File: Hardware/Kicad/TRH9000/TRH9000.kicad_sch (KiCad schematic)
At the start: 10 parts, among them U4 74VHC138, U5 T.I_SN74AHCT32D

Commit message: Started routing the PCB, adding cut-outs to separate the analog from digital signal-domains.
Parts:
- removed C11, C12: C_CC0805JPX7R9BB104, Capacitor_SMD:C_0805_2012Metric, symbol LRJ-parts:C_CC0805JPX7R9BB104
- removed C25, C26, C27: C_CL21B105KBFNNNF, Capacitor_SMD:C_0805_2012Metric_Pad1.18x1.45mm_HandSolder, symbol LRJ-parts:C_CL21B105KBFNNNF
- added C23: C_CL21B106KOQNNNE, Capacitor_SMD:C_0805_2012Metric, symbol LRJ-parts:C_CL21B106KOQNNNE
- added LOGO1: Logo_Open_Hardware_Small, Symbol:OSHW-Logo2_14.6x12mm_SilkScreen, symbol Graphic:Logo_Open_Hardware_Small
- BUS1: value MSX_SLOT_EDGE-CON -> MSX-CONN_L-P; footprint trh9000:msx_cartridge -> trh9000:msx_edge-conn-LP; symbol TRH9000:MSX_SLOT_EDGE-CON -> TRH9000:MSX-CONN_L-P
- Cart1: footprint trh9000:MSX-cart-dummy -> trh9000:MSX-cart-dummy_RA
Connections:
- net +5V: now also C23.1
- net GND: now also C23.2
- net ~{Y6}: now reaches U4.9 (~{Y6}), U5.2 (1B), U5.5 (2B)
- removed net +12V: BUS1.48 (+12V)
- removed net -12V: BUS1.50 (-12V)
- removed net ~{RFSH}: BUS1.6 (~{RFSH})
- no-connect marks 11 -> 12

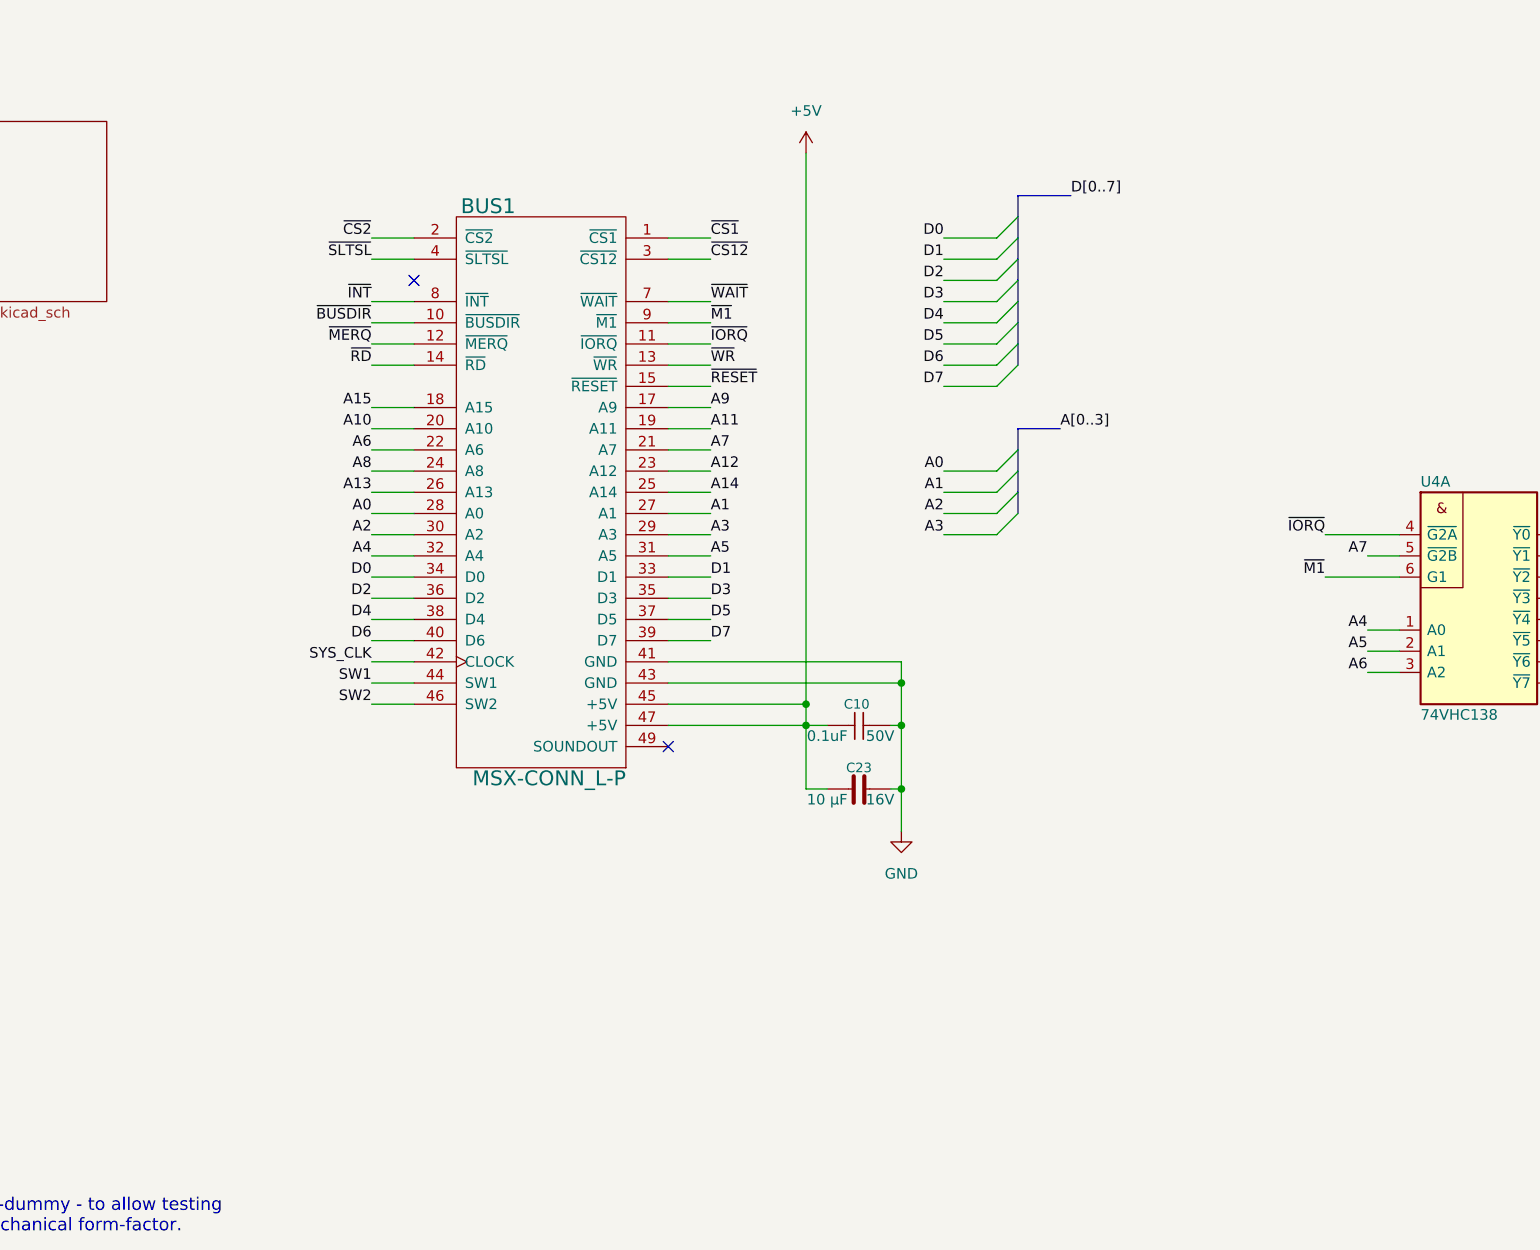
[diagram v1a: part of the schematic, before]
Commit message: More routing of the analog portion. Added 3D-models for the VGA and Scart connectors.
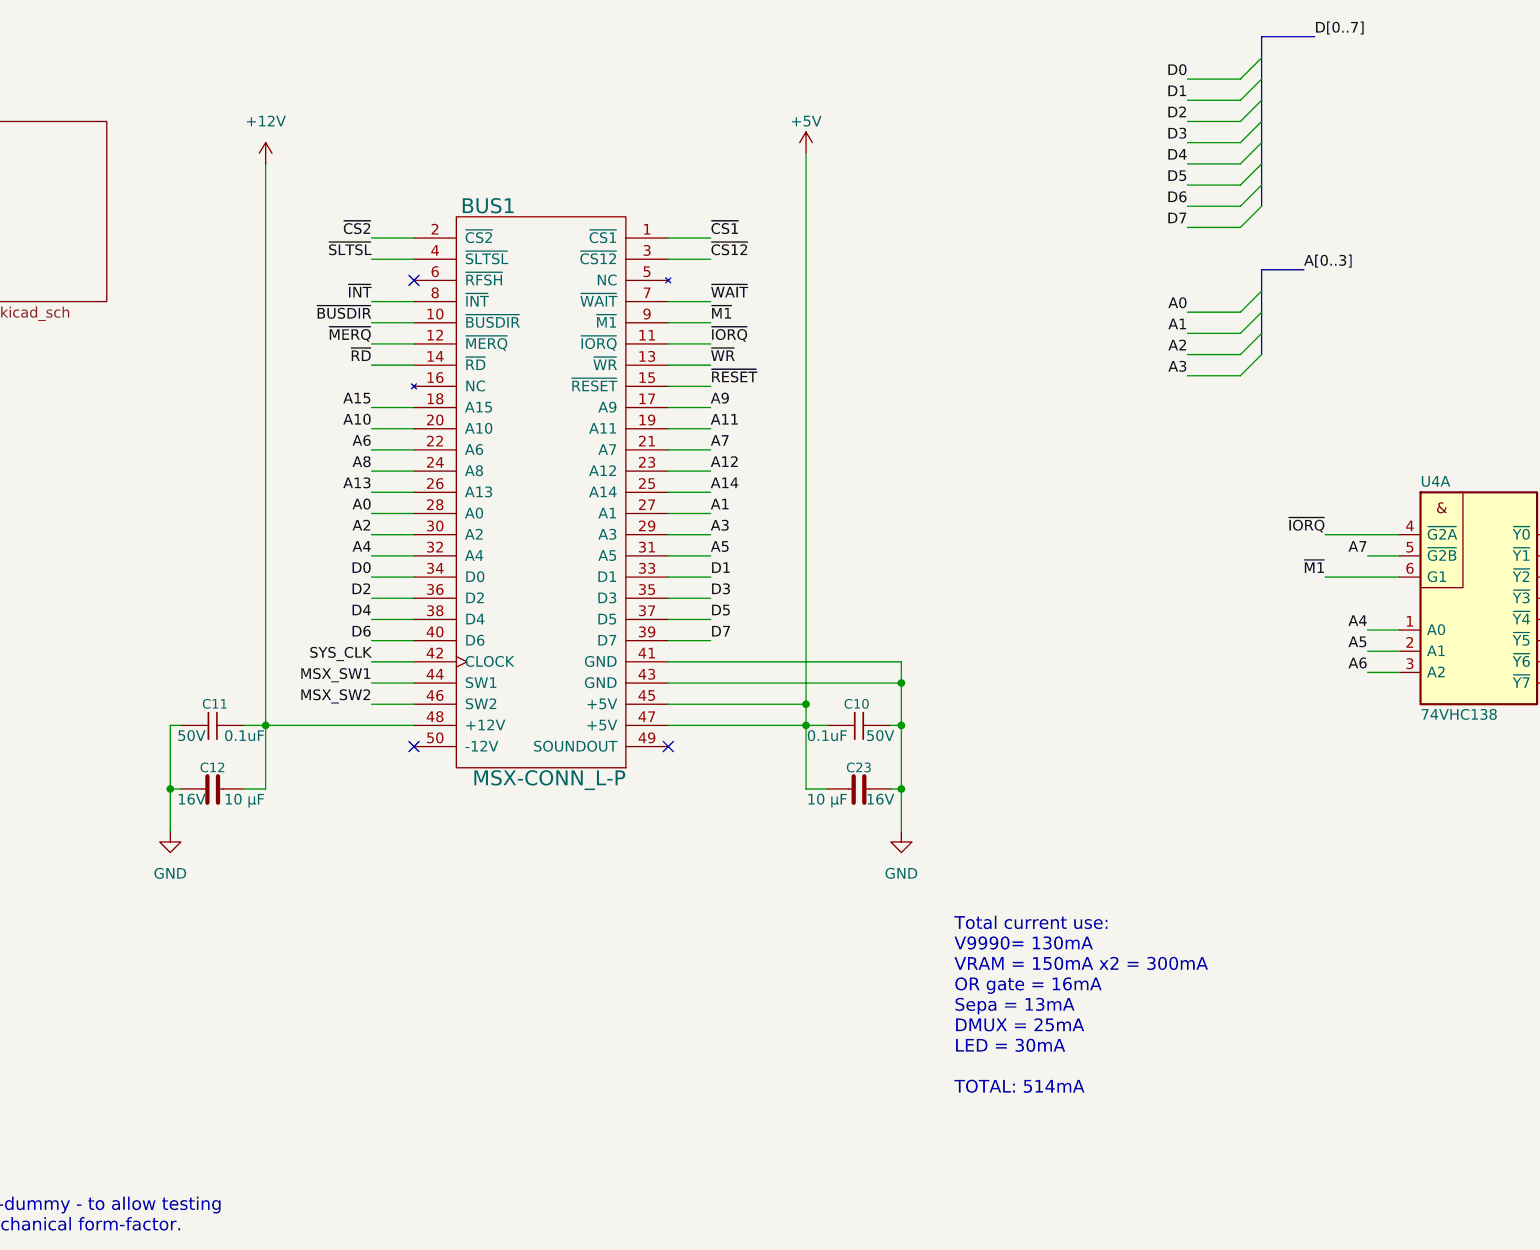
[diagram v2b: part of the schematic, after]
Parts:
- added C11: C_CC0805JPX7R9BB104, Capacitor_SMD:C_0805_2012Metric, symbol LRJ-parts:C_CC0805JPX7R9BB104
- added C12: C_CL21B106KOQNNNE, Capacitor_SMD:C_0805_2012Metric, symbol LRJ-parts:C_CL21B106KOQNNNE
- BUS1: footprint trh9000:msx_edge-conn-LP -> trh9000:msx_cart_edge-conn; symbol TRH9000:MSX-CONN_L-P -> TRH9000:MSX_SLOT_EDGE-CON
- C10: Price €0,14 -> (none)
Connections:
- net GND: now also C11.2, C12.2
- net SW1 renamed MSX_SW1
- net SW2 renamed MSX_SW2
- new net +12V: BUS1.48 (+12V), C11.1, C12.1
- no-connect marks 12 -> 13
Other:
- note added: "Total current use: V9990= 130mA VRAM = 150mA x2 = 300mA OR gate = 16mA Sepa = 13mA DMUX = 25mA LED = 30mA TOTAL: 514mA"

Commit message: Did a reroute of the analog / digital separation.
Did a reroute of the analog / digital separation.
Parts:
- added C22, C42: 47pF, Capacitor_SMD:C_0603_1608Metric, symbol Device:C
- added C41: C_CC0805JPX7R9BB104, Capacitor_SMD:C_0805_2012Metric, symbol LRJ-parts:C_CC0805JPX7R9BB104
- added C43: 47pF, LRJ:C_0603_1608Metric_round_court, symbol Device:C
- added C44: C_CL10B104KB8NNNL, LRJ:C_0603_1608Metric_round_court, symbol LRJ-parts:C_CL10B104KB8NNNL
- added J5: DIN-8_SD-80BV, LRJ:Jack_DIN_CUI_SD-80BV_Vertical, symbol LRJ-parts:DIN-8_SD-80BV
- added R22: 75, Resistor_SMD:R_0603_1608Metric, symbol Device:R
- added R23: 100, LRJ:R_0603_1608Metric_roundcourt, symbol Device:R
- added R30: R_RC0603FR-0710KL, LRJ:R_0603_1608Metric_roundcourt, symbol LRJ-parts:R_RC0603FR-0710KL
- added R31, R32: 100, Resistor_SMD:R_0603_1608Metric, symbol Device:R
- added R8: R_ERJ-3GEYJ105V, Resistor_SMD:R_0603_1608Metric, symbol LRJ-parts:R_ERJ-3GEYJ105V
- added U8: LMH1980, Package_SO:VSSOP-10_3x3mm_P0.5mm, symbol LRJ-parts:LMH1980
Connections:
- net GND: now also C22.2, C41.2, C42.2, C43.2, R22.2, R30.1, R8.1
- net SCIN: no longer names the net of U5.8 (3Y)
- removed net SYS_CLK: BUS1.42 (CLOCK), U5.10 (3B), U5.9 (3A)
- net ~{CS1}: no longer names the net of BUS1.1 (~{CS1})
- net ~{CS2}: no longer names the net of BUS1.2 (~{CS2})
- net ~{MERQ}: no longer names the net of BUS1.12 (~{MERQ})
- new net: C42.1, C43.1, C44.2, R23.1
- new net: J5.SH, R8.2
- new net Be: J5.8
- new net GNDe: C22.1, C41.1, J5.1
- new net Ge: J5.7
- new net HSOe: R31.2, U8.6 (HSOUT)
- new net REXTe: R30.2, U8.1 (REXT)
- new net Re: J5.6
- new net SOUNDOUT: J5.2
- new net V9958_HSYNC: R31.1
- new net V9958_VSYNC: R32.1
- new net VSOe: R32.2, U8.7 (VSOUT)
- new net ~{CSYNCe_}: C44.1, U8.4 (VIN)
- new net ~{CSYNCe}: J5.4, R22.1, R23.2
- new net ~{YSe}: J5.5
- no-connect marks 13 -> 25
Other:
- sheet VDP ports: added Bi, Gi, Ri, V9958_HSYNC, V9958_VSYNC, ~{CSYNCi}, ~{YSi}; removed B, G, R, ~{CSYNC}
- sheet VIDEO ports: added Be, Bi, Ge, Gi, Re, Ri, SOUNDOUT, ~{CSYNCi}, ~{YSe}, ~{YSi}; removed B, G, R, SCIN, ~{CSYNC}
- note added: "1. Super-impose circuitry"
- note added: "1.1. MSX standard RGB connector"
- note added: "1.2. Sync Separator (external)"
- note added: "3. AV AV Control (+4.5V to +5V) To SCART pin 8"
- note added: "Implementing Superimpose: ----------------------- v-1. Feed external HSYNC / VSYNC into V9990 HRESET / VRESET pins for synchronisation v-2. Combine external and internal R, G, B with an analog multiplexer, controlled by /Ys signal (Chip Select) The principle is that the original external signal is passed through while /Ys is not superimposing."
- note added: "LEGEND: ------ VDP = Video Display Processor CLK = Clock SLTSL = Slot Select signal CS = Chip Select SYS_CLK = MSX System Clock Re, Ge, Be = RGB External"
- note added: "~{CS1}"
- note added: "~{CS2}"
- note added: "~{MERQ}"
- note removed: "LEGEND: ------ VDP = Video Display Processor CLK = Clock SLTSL = Slot Select signal CS = Chip Select SYS_CLK = MSX System Clock"
- note removed: "Total current use: V9990= 130mA VRAM = 150mA x2 = 300mA OR gate = 16mA Sepa = 13mA DMUX = 25mA LED = 30mA TOTAL: 514mA"
- moved on the sheet: Cart1

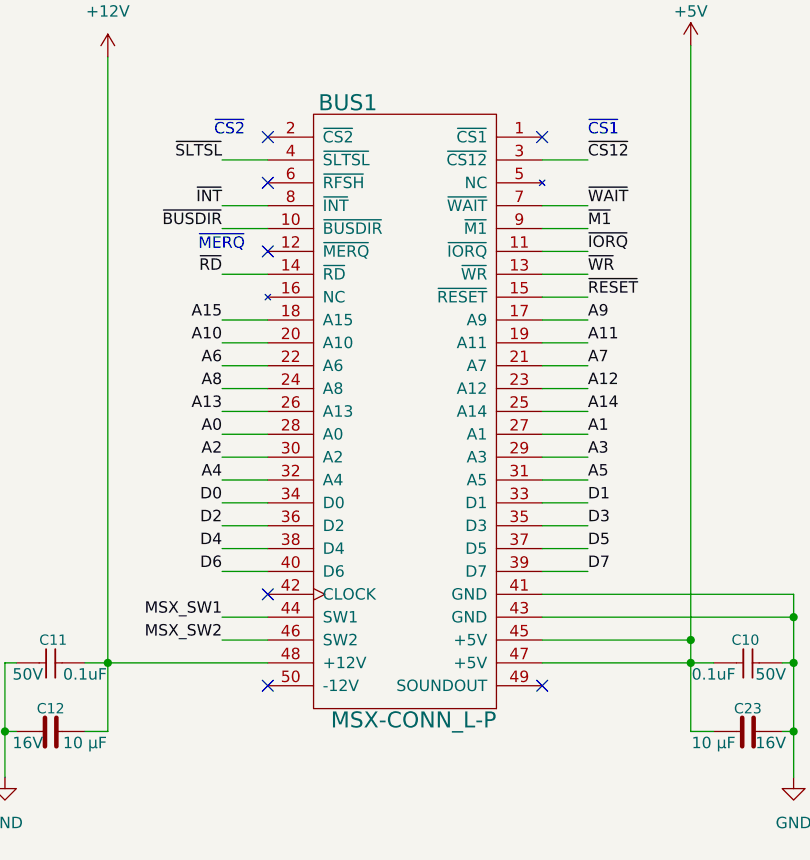
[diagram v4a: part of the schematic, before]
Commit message: More routing - almost finished - only 29 more lines to go...
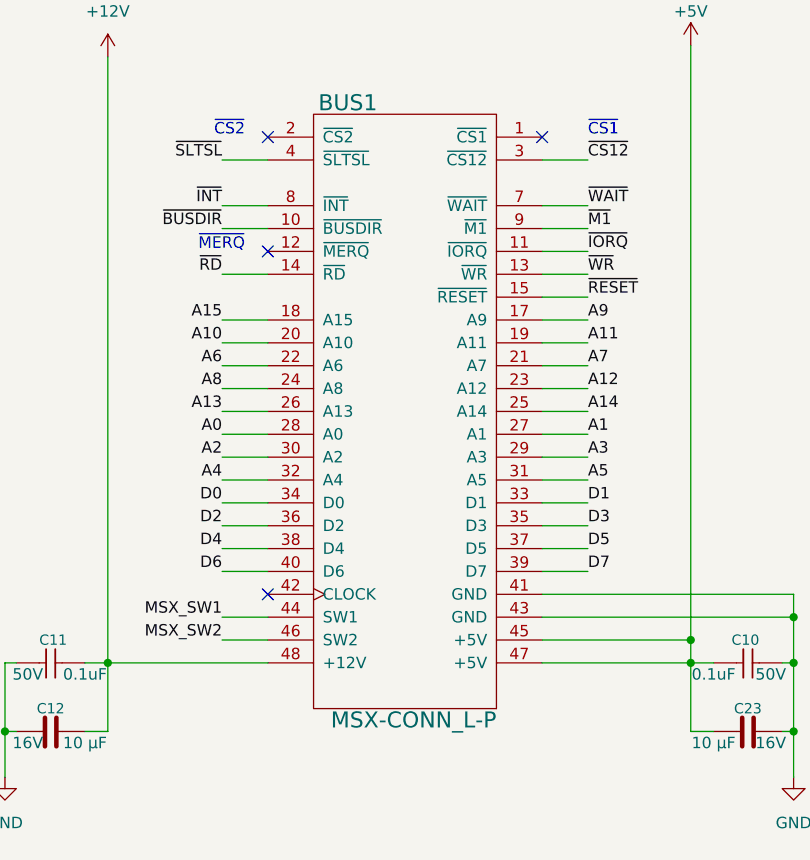
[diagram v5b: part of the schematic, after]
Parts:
- BUS1: footprint trh9000:msx_cart_edge-conn -> trh9000:msx_edge-conn-LP; symbol TRH9000:MSX_SLOT_EDGE-CON -> TRH9000:MSX-CONN_L-P
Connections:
- no-connect marks 25 -> 22
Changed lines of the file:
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@@
   (no_connect (at 87.63 46.99))
   (no_connect (at 231.14 185.42))
-  (no_connect (at 87.63 52.07))
-  (no_connect (at 87.63 107.95))
   (no_connect (at 231.14 172.72))
   (no_connect (at 247.65 100.33))
   (no_connect (at 247.65 97.79))
   (no_connect (at 267.97 100.33))
-  (no_connect (at 118.11 107.95))
   (no_connect (at 118.11 46.99))
   (bus_entry (at 189.23 58.42) (size -2.54 2.54)
@@
     (pin "2")
   )
-  (symbol (lib_id "TRH9000:MSX_SLOT_EDGE-CON") (at 102.87 77.47 0) (mirror y) (unit 1)
+  (symbol (lib_id "TRH9000:MSX-CONN_L-P") (at 102.87 77.47 0) (mirror y) (unit 1)
     (in_bom no) (on_board yes)
     (property "Reference" "BUS1" (id 0) (at 96.52 43.18 0)
@@
       (effects (font (size 1.778 1.778)) (justify left))
     )
-    (property "Footprint" "trh9000:msx_cart_edge-conn" (id 2) (at 102.87 115.57 0)
+    (property "Footprint" "trh9000:msx_edge-conn-LP" (id 2) (at 102.87 115.57 0)
       (effects (font (size 1.524 1.524)) hide)
     )
@@
     (pin "14")
     (pin "15")
-    (pin "16")
     (pin "17")
     (pin "18")
@@
     (pin "47")
     (pin "48")
-    (pin "49")
-    (pin "5")
-    (pin "50")
-    (pin "6")
     (pin "7")
     (pin "8")
@@
       (reference "#PWR0109") (unit 1) (value "+12VA") (footprint "")
     )
+    (path "/d5c7e94e-ee8c-4fa2-b6f9-333fadc34caa/41c93a84-8d81-4e2d-aa46-d4a61cae6f9a"
+      (reference "#PWR0110") (unit 1) (value "+5VA") (footprint "")
+    )
+    (path "/d5c7e94e-ee8c-4fa2-b6f9-333fadc34caa/695f3bf4-7c7a-4d75-9282-0517399ad128"
+      (reference "#PWR0111") (unit 1) (value "+5VA") (footprint "")
+    )
     (path "/d5c7e94e-ee8c-4fa2-b6f9-333fadc34caa/cfc2eec3-ed8d-43b5-b7e7-3e7d6fb4985b"
       (reference "#PWR0115") (unit 1) (value "GND") (footprint "")
@@
       (reference "#PWR0151") (unit 1) (value "GND") (footprint "")
     )
-    (path "/d5c7e94e-ee8c-4fa2-b6f9-333fadc34caa/41c93a84-8d81-4e2d-aa46-d4a61cae6f9a"
-      (reference "#PWR?") (unit 1) (value "+5VA") (footprint "")
-    )
-    (path "/d5c7e94e-ee8c-4fa2-b6f9-333fadc34caa/695f3bf4-7c7a-4d75-9282-0517399ad128"
-      (reference "#PWR?") (unit 1) (value "+5VA") (footprint "")
-    )
     (path "/d5c7e94e-ee8c-4fa2-b6f9-333fadc34caa/8b3f5935-84e1-400b-9e2c-a3b091295e00"
       (reference "#SYM1") (unit 1) (value "SYM_Arrow45_Small") (footprint "")
@@
     )
     (path "/edcf146e-8434-4b34-9742-8eb99e522d20"
-      (reference "BUS1") (unit 1) (value "MSX-CONN_L-P") (footprint "trh9000:msx_cart_edge-conn")
+      (reference "BUS1") (unit 1) (value "MSX-CONN_L-P") (footprint "trh9000:msx_edge-conn-LP")
     )
     (path "/d5c7e94e-ee8c-4fa2-b6f9-333fadc34caa/8d255c9b-c893-4e62-abb1-0b6fcc8981b9"
@@
     )
     (path "/d9ed34ef-ff83-4a70-a9f7-db0f42d1292e/1b4ca6cb-8997-4c16-a74a-6a6ca4edb901"
-      (reference "C2") (unit 1) (value "C_CC0805JPX7R9BB104") (footprint "Capacitor_SMD:C_0805_2012Metric")
+      (reference "C2") (unit 1) (value "C_CC0805JPX7R9BB104") (footprint "LRJ:C_0805_2012Metric_round_court")
     )
     (path "/bc7b9d52-219c-453a-9752-d4491f369786/6f23a65c-1b2d-489a-b128-681a79a31886"
@@
     )
     (path "/d5c7e94e-ee8c-4fa2-b6f9-333fadc34caa/6f712bc1-4eb0-439a-a5fd-bb1c6396a84d"
-      (reference "Y1") (unit 1) (value "Y_HCM4921477270ABJT") (footprint "LRJ:Crystal_HC49-US_Vertical")
-    )
-  )
+      (reference "Y1") (unit 1) (value "Y_HCM4921477270ABJT") (footprint "trh9000:Crystal_HC49-US_Vertical_cy_mod")
+    )
+  )

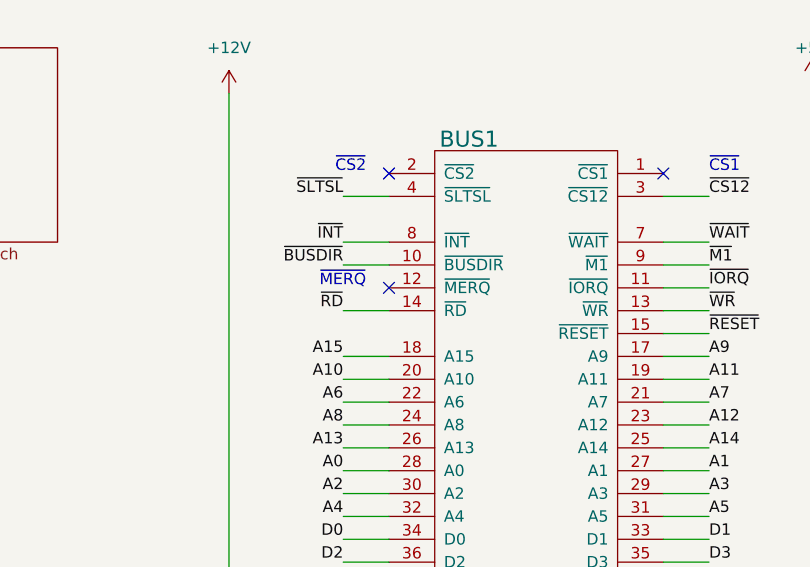
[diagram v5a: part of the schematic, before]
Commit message: Replaced insulation-cutouts with round ones, as special shapes cost more to manufacture. Only 26 lines left to route...
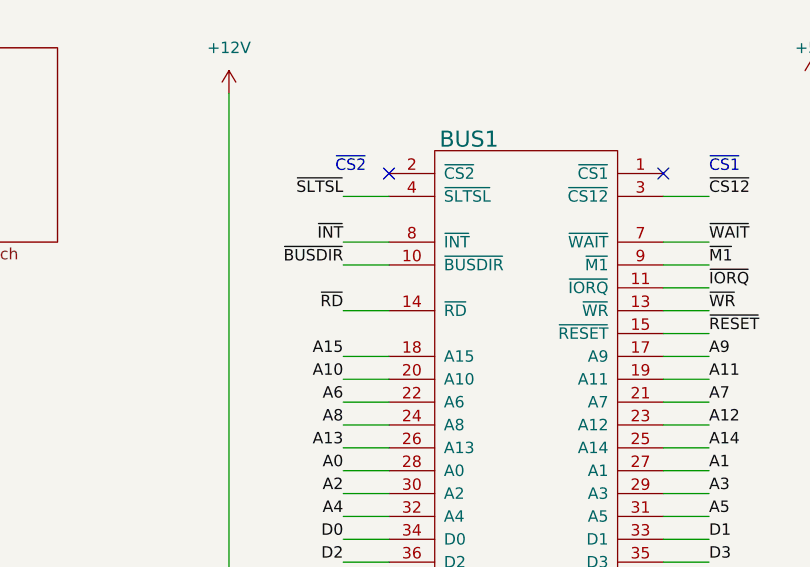
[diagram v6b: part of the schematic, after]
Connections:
- no-connect marks 22 -> 21
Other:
- note removed: "~{MERQ}"
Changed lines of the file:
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@@
   (no_connect (at 231.14 182.88))
   (no_connect (at 231.14 180.34))
-  (no_connect (at 87.63 59.69))
   (no_connect (at 247.65 92.71))
   (no_connect (at 247.65 95.25))
@@
     (stroke (width 0) (type default) (color 0 0 0 0))
   )
-  (text "~{MERQ}" (at 85.09 59.69 180)
-    (effects (font (size 1.27 1.27)) (justify right bottom))
-  )
   (text "1.1. MSX standard RGB connector" (at 104.14 157.48 0)
     (effects (font (size 1.524 1.524)) (justify left bottom))
@@
     (pin "10")
     (pin "11")
-    (pin "12")
     (pin "13")
     (pin "14")
